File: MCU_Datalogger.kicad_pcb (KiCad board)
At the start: 2 copper layers, 27 parts, among them J1 Conn_01x04_Pin, J2 Conn_01x04_Pin, J3 Conn_01x09_Pin, J4 Conn_02x03_Odd_Even, U1 24LC1025, U2 24LC1025, Y1 32.768 KHz, Y2 16 MHz

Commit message: Wiring Main
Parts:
- added U3: DS1337S_, DS1337S_:SOIC127P600X175-8N, F.Cu at (79.8, 82.8)
- added U4: ATMEGA328P-AU, ATMEGA328P-AU:QFP80P900X900X120-32N, F.Cu at (79.4, 66.4)

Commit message: Rout
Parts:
- moved U4 85.1 mm to (162.5, 85.0)
- moved U3 68.5 mm to (148.0, 88.5)
- moved H3 63.1 mm to (185.0, 72.5)
- moved H4 62.4 mm to (185.0, 97.5)
- moved R7 52.1 mm to (177.8, 73.0), turned to 180 degrees
- moved R5 43.7 mm to (172.0, 83.0)
- moved C5 40.8 mm to (172.8, 74.2), turned to -90 degrees
- moved C3 40.2 mm to (170.0, 93.5), turned to 90 degrees
- moved D2 39.4 mm to (177.8, 77.8), turned to 180 degrees
- moved C2 37.5 mm to (165.5, 93.5), turned to 180 degrees
- moved D1 36.1 mm to (177.8, 82.8)
- moved C4 35.8 mm to (168.2, 74.2), turned to -90 degrees
- moved R6 33.2 mm to (159.2, 74.5), turned to -90 degrees
- moved J4 30.9 mm to (185.5, 81.8), turned to 180 degrees
- moved J1 30.9 mm to (171.8, 98.2), turned to 90 degrees
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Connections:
- BT1 pad 1: unconnected-(BT1-+-Pad1) -> Net-(BT1-+)
- BT1 pad 2: unconnected-(BT1---Pad2) -> GND
- C1 pad 1: unconnected-(C1-Pad1) -> /VCC
- C1 pad 2: unconnected-(C1-Pad2) -> GND
- C2 pad 1: unconnected-(C2-Pad1) -> Net-(U4-PB6)
- C2 pad 2: unconnected-(C2-Pad2) -> GND
- C3 pad 1: unconnected-(C3-Pad1) -> GND
- C3 pad 2: unconnected-(C3-Pad2) -> Net-(U4-PB7)
- C4 pad 1: unconnected-(C4-Pad1) -> GND
- C4 pad 2: unconnected-(C4-Pad2) -> Net-(U4-AREF)
- C5 pad 1: unconnected-(C5-Pad1) -> Net-(BT1-+)
- C5 pad 2: unconnected-(C5-Pad2) -> GND
- D1 pad 1: unconnected-(D1-K-Pad1) -> Net-(D1-K)
- D1 pad 2: unconnected-(D1-A-Pad2) -> /SCK
- D2 pad 1: unconnected-(D2-K-Pad1) -> Net-(D2-K)
- D2 pad 2: unconnected-(D2-A-Pad2) -> Net-(BT1-+)
- J1 pad 1: unconnected-(J1-Pin_1-Pad1) -> GND
- J1 pad 2: unconnected-(J1-Pin_2-Pad2) -> /VCC
- J1 pad 3: unconnected-(J1-Pin_3-Pad3) -> /SDA
- J1 pad 4: unconnected-(J1-Pin_4-Pad4) -> /SCK
- J2 pad 1: unconnected-(J2-Pin_1-Pad1) -> GND
- J2 pad 2: unconnected-(J2-Pin_2-Pad2) -> /VCC
- J2 pad 3: unconnected-(J2-Pin_3-Pad3) -> /RX
- J2 pad 4: unconnected-(J2-Pin_4-Pad4) -> /TX
- J3 pad 1: unconnected-(J3-Pin_1-Pad1) -> /D2
- J3 pad 2: unconnected-(J3-Pin_2-Pad2) -> /D3
- J3 pad 3: unconnected-(J3-Pin_3-Pad3) -> /D4
- J3 pad 4: unconnected-(J3-Pin_4-Pad4) -> /D5
- J3 pad 5: unconnected-(J3-Pin_5-Pad5) -> /D6
- J3 pad 6: unconnected-(J3-Pin_6-Pad6) -> /D7
- J3 pad 7: unconnected-(J3-Pin_7-Pad7) -> /D8
- J3 pad 8: unconnected-(J3-Pin_8-Pad8) -> GND
- J3 pad 9: unconnected-(J3-Pin_9-Pad9) -> /VCC
- J4 pad 1: unconnected-(J4-Pin_1-Pad1) -> /MISO
- J4 pad 2: unconnected-(J4-Pin_2-Pad2) -> /VCC
- J4 pad 3: unconnected-(J4-Pin_3-Pad3) -> /SCK
- J4 pad 4: unconnected-(J4-Pin_4-Pad4) -> /MOSI
- J4 pad 5: unconnected-(J4-Pin_5-Pad5) -> /RESET
- J4 pad 6: unconnected-(J4-Pin_6-Pad6) -> GND
- R1 pad 1: unconnected-(R1-Pad1) -> /VCC
- R1 pad 2: unconnected-(R1-Pad2) -> Net-(U3-~{INTA})
- R2 pad 1: unconnected-(R2-Pad1) -> /VCC
- R2 pad 2: unconnected-(R2-Pad2) -> Net-(U3-SQW/~INT)
- R3 pad 1: unconnected-(R3-Pad1) -> /VCC
- R3 pad 2: unconnected-(R3-Pad2) -> /SCK
- R4 pad 1: unconnected-(R4-Pad1) -> /SDA
- R4 pad 2: unconnected-(R4-Pad2) -> /VCC
- R5 pad 1: unconnected-(R5-Pad1) -> GND
- R5 pad 2: unconnected-(R5-Pad2) -> Net-(D1-K)
- R6 pad 1: unconnected-(R6-Pad1) -> /VCC
- R6 pad 2: unconnected-(R6-Pad2) -> /RESET
- R7 pad 1: unconnected-(R7-Pad1) -> Net-(D2-K)
- R7 pad 2: unconnected-(R7-Pad2) -> GND
- U1 pad 1: unconnected-(U1-A0-Pad1) -> /VCC
- U1 pad 2: unconnected-(U1-A1-Pad2) -> /VCC
- U1 pad 3: unconnected-(U1-A2-Pad3) -> /VCC
- U1 pad 4: unconnected-(U1-GND-Pad4) -> GND
- U1 pad 5: unconnected-(U1-SDA-Pad5) -> /SDA
- U1 pad 6: unconnected-(U1-SCL-Pad6) -> /SCK
- U1 pad 7: unconnected-(U1-WP-Pad7) -> GND
- U1 pad 8: unconnected-(U1-VCC-Pad8) -> /VCC
- U2 pad 1: unconnected-(U2-A0-Pad1) -> /VCC
- U2 pad 2: unconnected-(U2-A1-Pad2) -> GND
- U2 pad 3: unconnected-(U2-A2-Pad3) -> /VCC
- U2 pad 4: unconnected-(U2-GND-Pad4) -> GND
- U2 pad 5: unconnected-(U2-SDA-Pad5) -> /SDA
- U2 pad 6: unconnected-(U2-SCL-Pad6) -> /SCK
- U2 pad 7: unconnected-(U2-WP-Pad7) -> GND
- U2 pad 8: unconnected-(U2-VCC-Pad8) -> /VCC
- U3 pad 1: unconnected-(U3-X1-Pad1) -> Net-(U3-X1)
- U3 pad 2: unconnected-(U3-X2-Pad2) -> Net-(U3-X2)
- U3 pad 3: unconnected-(U3-~{INTA}-Pad3) -> Net-(U3-~{INTA})
- U3 pad 4: unconnected-(U3-GND-Pad4) -> GND
- U3 pad 5: unconnected-(U3-SDA-Pad5) -> /SDA
- U3 pad 6: unconnected-(U3-SCL-Pad6) -> /SCK
- U3 pad 7: unconnected-(U3-SQW/~INT-Pad7) -> Net-(U3-SQW/~INT)
- U3 pad 8: unconnected-(U3-VCC-Pad8) -> /VCC
- U4 pad 1: unconnected-(U4-PD3-Pad1) -> /D3
- U4 pad 10: unconnected-(U4-PD6-Pad10) -> /D6
- U4 pad 11: unconnected-(U4-PD7-Pad11) -> /D7
- U4 pad 12: unconnected-(U4-PB0-Pad12) -> /D8
- U4 pad 15: unconnected-(U4-PB3-Pad15) -> /MOSI
- U4 pad 16: unconnected-(U4-PB4-Pad16) -> /MISO
- U4 pad 17: unconnected-(U4-PB5-Pad17) -> /SCK
- U4 pad 18: unconnected-(U4-AVCC-Pad18) -> Net-(BT1-+)
- U4 pad 2: unconnected-(U4-PD4-Pad2) -> /D4
- U4 pad 20: unconnected-(U4-AREF-Pad20) -> Net-(U4-AREF)
- U4 pad 21: unconnected-(U4-GND__2-Pad21) -> GND
- U4 pad 27: unconnected-(U4-PC4-Pad27) -> /SDA
- U4 pad 28: unconnected-(U4-PC5-Pad28) -> /SCK
- U4 pad 29: unconnected-(U4-PC6/~{RESET}-Pad29) -> /RESET
- U4 pad 3: unconnected-(U4-GND-Pad3) -> GND
- U4 pad 30: unconnected-(U4-PD0-Pad30) -> /RX
- U4 pad 31: unconnected-(U4-PD1-Pad31) -> /TX
- U4 pad 32: unconnected-(U4-PD2-Pad32) -> /D2
- U4 pad 5: unconnected-(U4-GND__1-Pad5) -> GND
- U4 pad 6: unconnected-(U4-VCC__1-Pad6) -> Net-(BT1-+)
- U4 pad 7: unconnected-(U4-PB6-Pad7) -> Net-(U4-PB6)
- U4 pad 8: unconnected-(U4-PB7-Pad8) -> Net-(U4-PB7)
- U4 pad 9: unconnected-(U4-PD5-Pad9) -> /D5
- Y1 pad 1: unconnected-(Y1-Pad1) -> Net-(U3-X2)
- Y1 pad 2: unconnected-(Y1-Pad2) -> Net-(U3-X1)
- Y2 pad 1: unconnected-(Y2-Pad1) -> Net-(U4-PB7)
- Y2 pad 2: unconnected-(Y2-Pad2) -> Net-(U4-PB6)
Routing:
- net GND: track 0.00 -> 156.2 mm, vias 0 -> 4
- net /VCC: track 0.00 -> 142.2 mm, vias 0 -> 3
- net /SDA: track 0.00 -> 101.2 mm, vias 0 -> 2
- net /SCK: track 0.00 -> 100.3 mm
- net Net-(BT1-+): track 0.00 -> 77.4 mm, vias 0 -> 3
- net /RESET: track 0.00 -> 37.6 mm, vias 0 -> 2
- net /TX: track 0.00 -> 32.8 mm, vias 0 -> 2
- net /RX: track 0.00 -> 30.3 mm, vias 0 -> 2
- net /D2: track 0.00 -> 26.2 mm, vias 0 -> 1
- net /MOSI: track 0.00 -> 24.5 mm, vias 0 -> 1
- net /MISO: track 0.00 -> 23.7 mm
- net /D3: track 0.00 -> 22.7 mm, vias 0 -> 1
- net /D4: track 0.00 -> 22.7 mm, vias 0 -> 1
- net Net-(U4-PB6): track 0.00 -> 22.2 mm
- net Net-(U4-PB7): track 0.00 -> 17.4 mm
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- added copper zone on F.Cu, net /VCC
- added copper zone on B.Cu, net GND
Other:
- board outline added: 50 x 30.2 mm

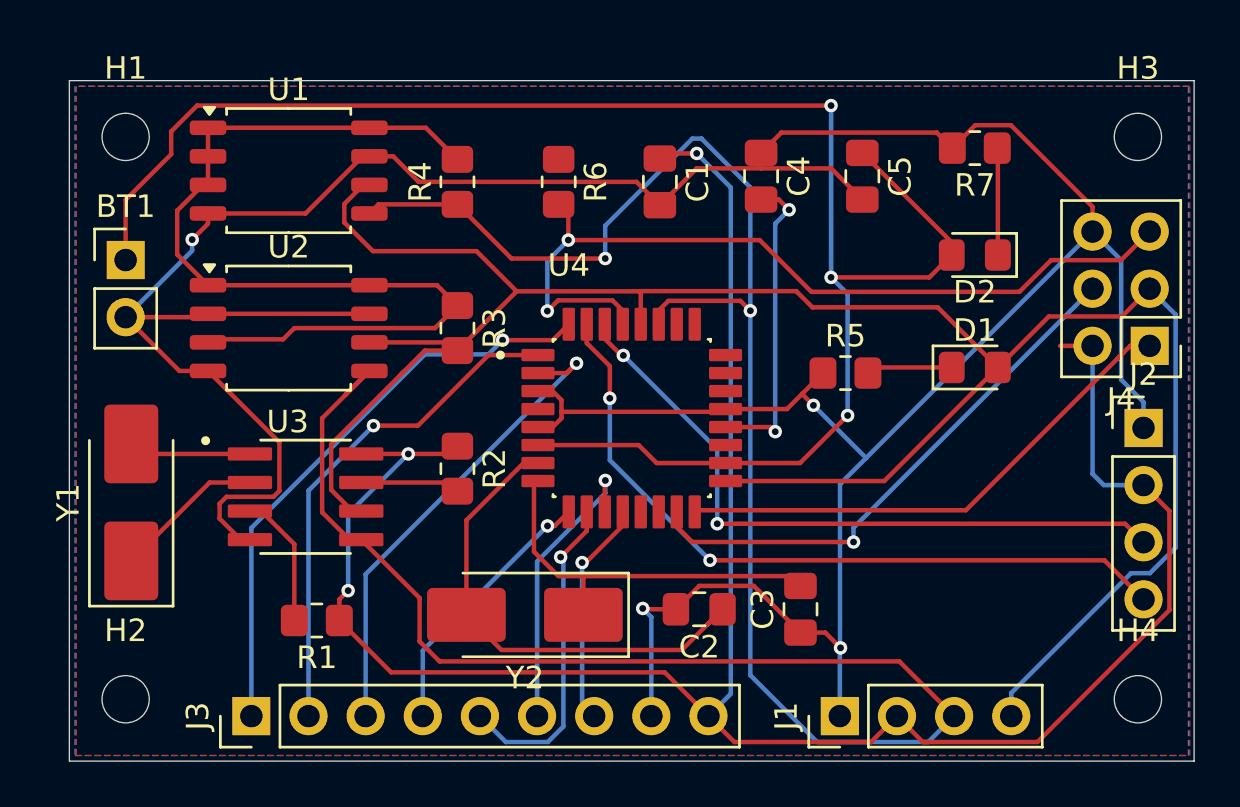
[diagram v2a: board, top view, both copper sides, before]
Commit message: Completed 2-layer
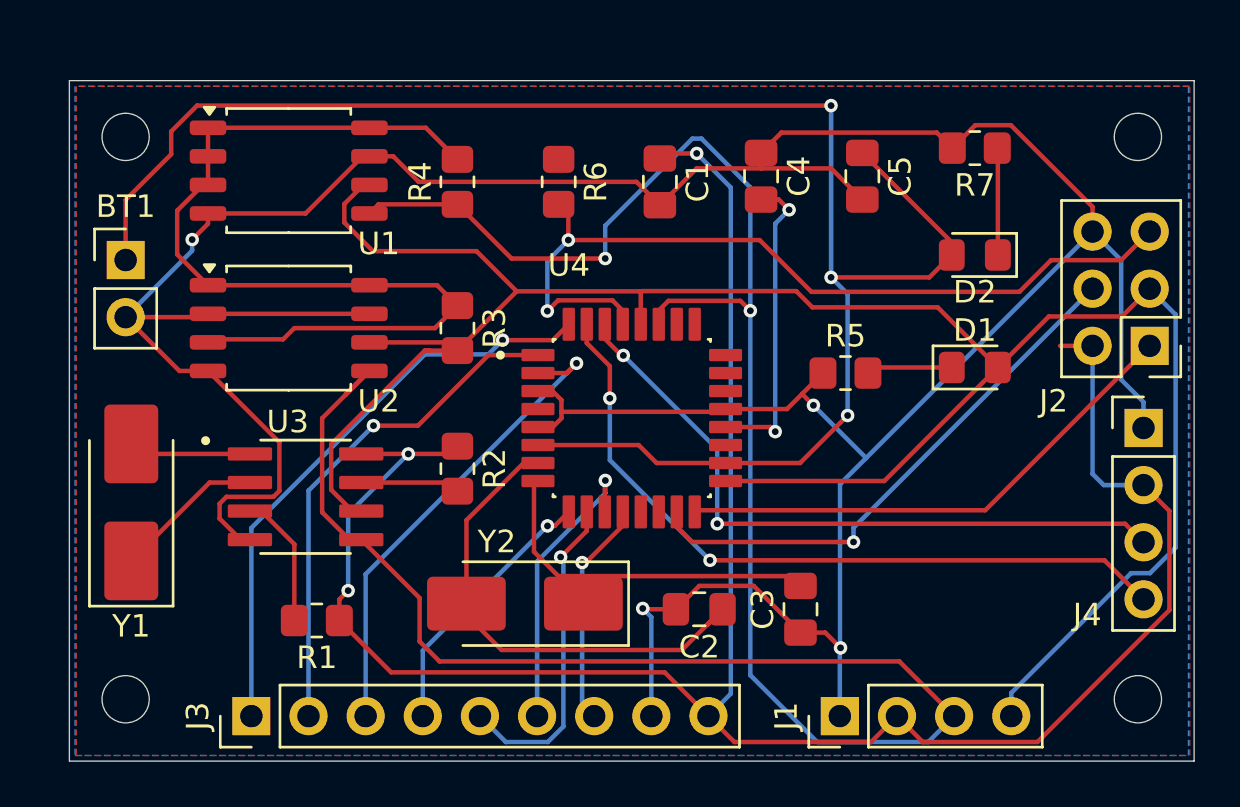
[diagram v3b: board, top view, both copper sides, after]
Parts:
- moved Y2 0.50 mm to (157.8, 93.2)
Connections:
- BT1 pad 1: Net-(BT1-+) -> /VCC
- C5 pad 1: Net-(BT1-+) -> /VCC
- D2 pad 2: Net-(BT1-+) -> /VCC
- U4 pad 18: Net-(BT1-+) -> /VCC
- U4 pad 6: Net-(BT1-+) -> /VCC
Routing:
- net Net-(BT1-+): track 77.4 -> 0.00 mm, vias 3 -> 0
- net /VCC: track 142.2 -> 219.6 mm, vias 3 -> 6
- net Net-(U4-PB7): track 17.4 -> 16.9 mm

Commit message: Solved Wire
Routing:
- net /VCC: track 219.6 -> 220.2 mm
- net Net-(U4-AREF): track 14.4 -> 13.8 mm
